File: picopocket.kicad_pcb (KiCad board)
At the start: 4 copper layers, 65.6 x 41.4 mm, 88 parts, among them IC1 AR1021, J1 Conn_02x40_Odd_Even, J2 Touchscreen, J3 Audio, Q1 BSS138, Q2 BSS138, U10 74LVC1G08, U11 74LVC1G34, U12 74LVC1G34, U13 74LVC32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

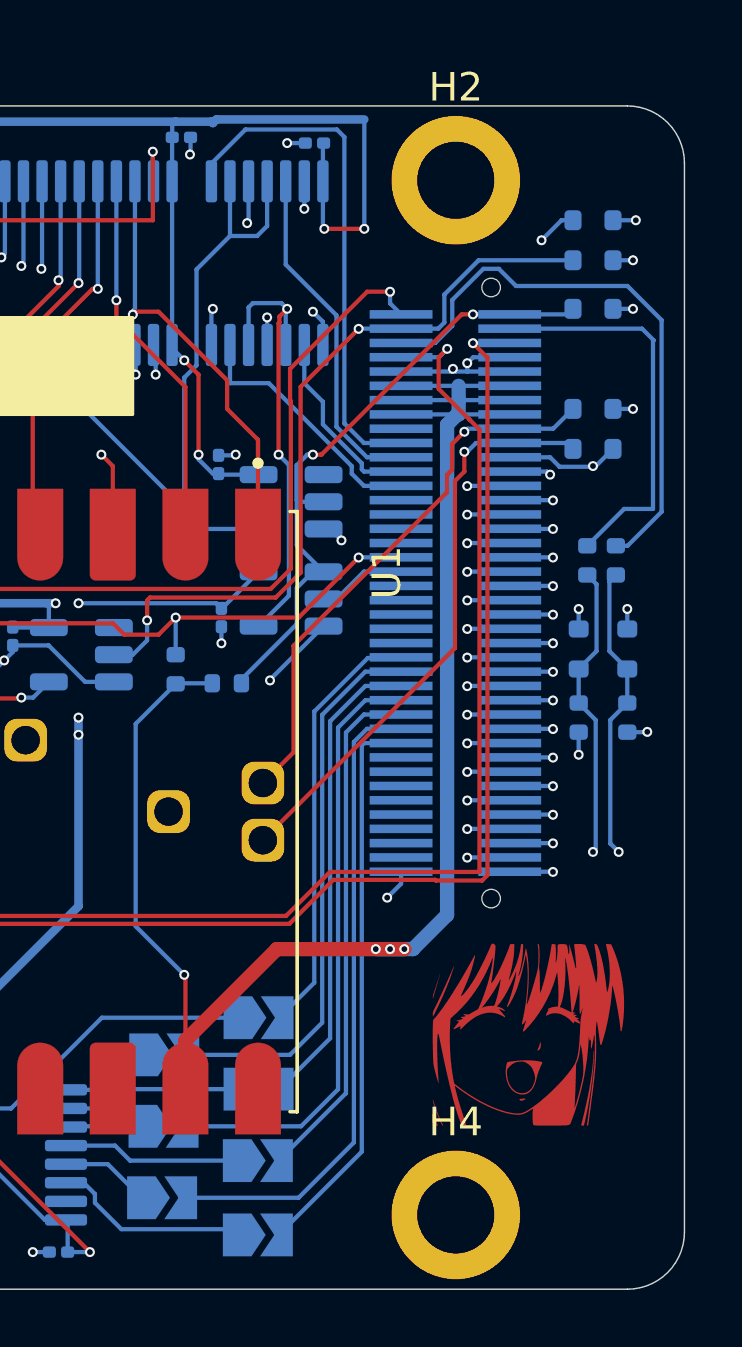
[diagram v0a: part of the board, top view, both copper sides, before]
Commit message: Update footprint to match exactly one on serial card
Thanks HeathenUK
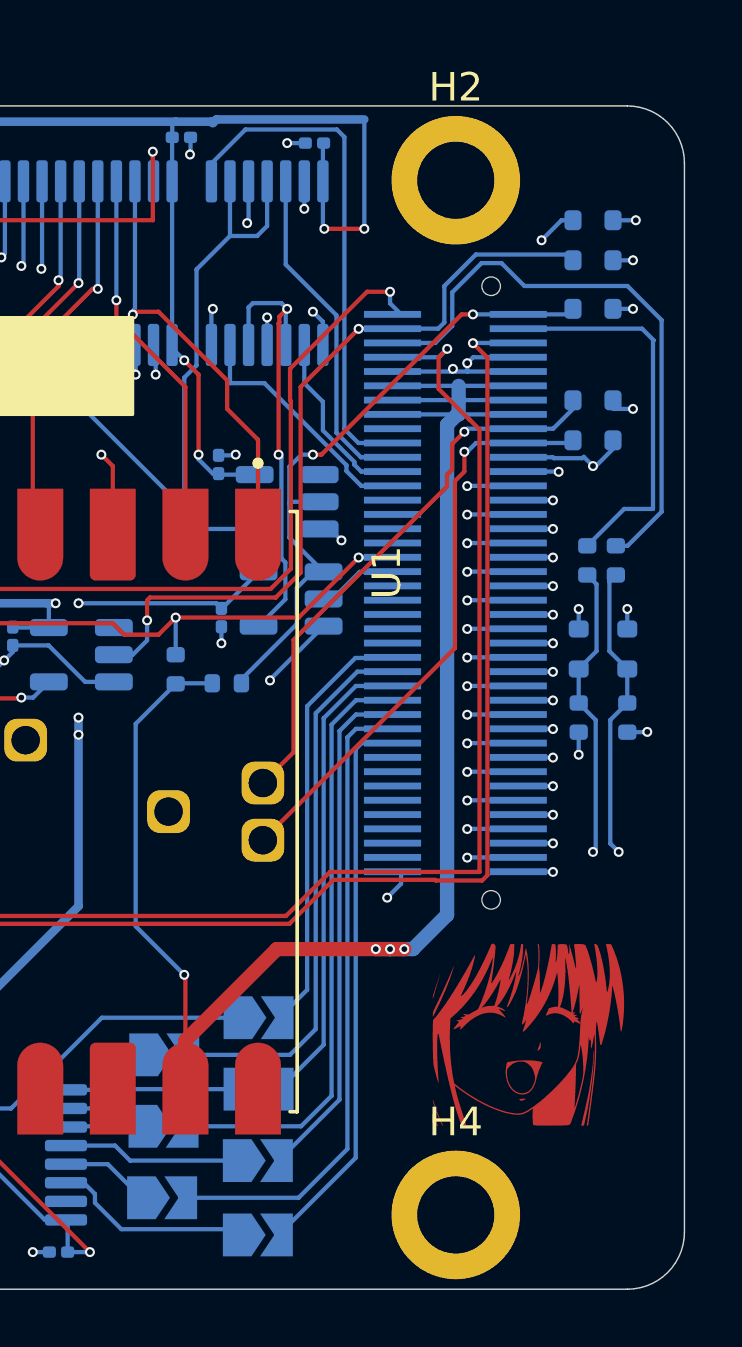
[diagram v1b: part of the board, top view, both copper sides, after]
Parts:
- moved D5 0.30 mm to (199.4, 95.8)
- moved D6 0.30 mm to (199.4, 97.2)
- moved U9 0.14 mm to (188.7, 99.3)
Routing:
- net ~{SMEMR}: track 12.0 -> 13.0 mm
- net DACK1: track 23.7 -> 23.1 mm
- net A0: track 17.8 -> 18.3 mm

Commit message: Add jlcpcb part numbers
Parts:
- U6: value APS6404L-3SQR-SN -> LY68L6400SLIT
